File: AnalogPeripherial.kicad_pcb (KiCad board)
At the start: 2 copper layers, 48 parts, among them J1 USART, J2 SWD, J3 USB_B_Mini, SW3 SW_Nidec_CAS-120A1, U1 LD1117S33TR_SOT223, U2 STM32F373CCTx, U3 LM386, U4 112J-TDAR-R01, U5 TLV9061xDBV, Y1 Crystal

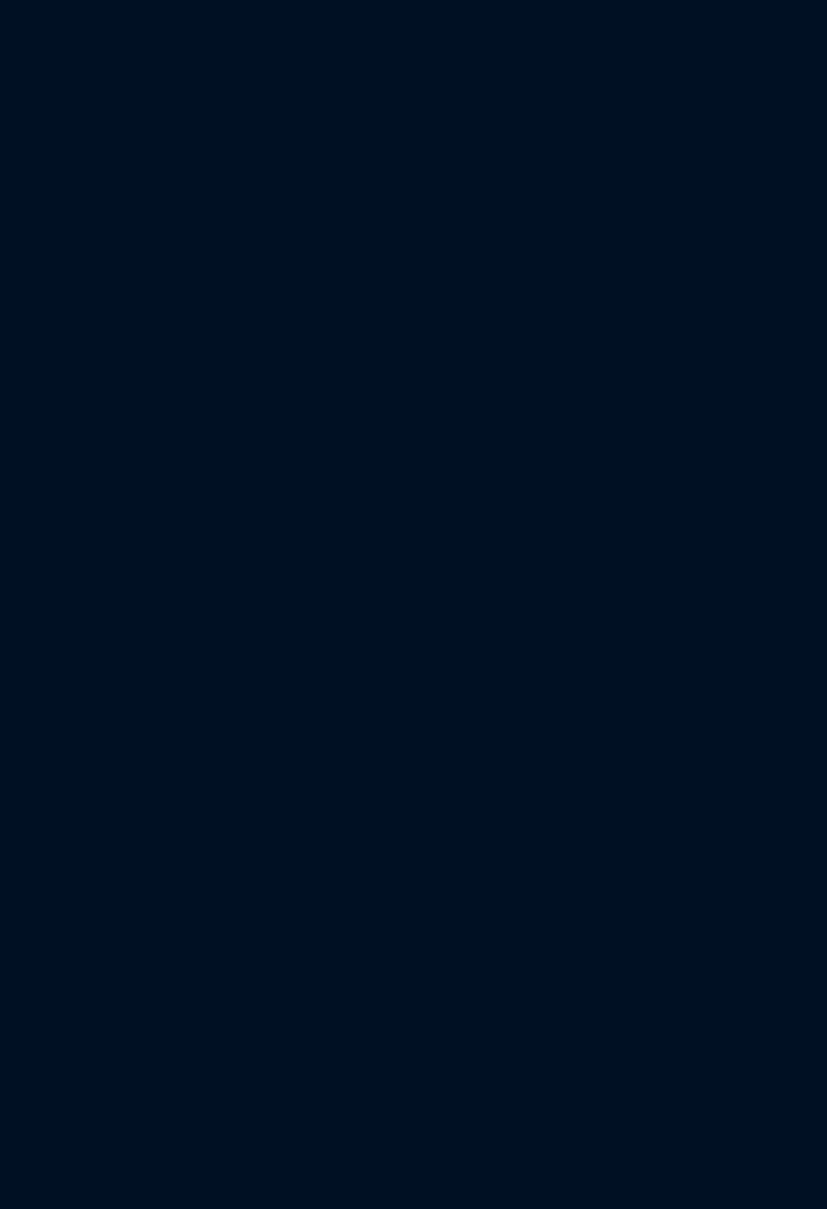
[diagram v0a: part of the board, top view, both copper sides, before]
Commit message: Add all footprint To do: 1. Add footprint and symbol to SD Card 2. Correct footprints and symobols 3. Finish the PCB design
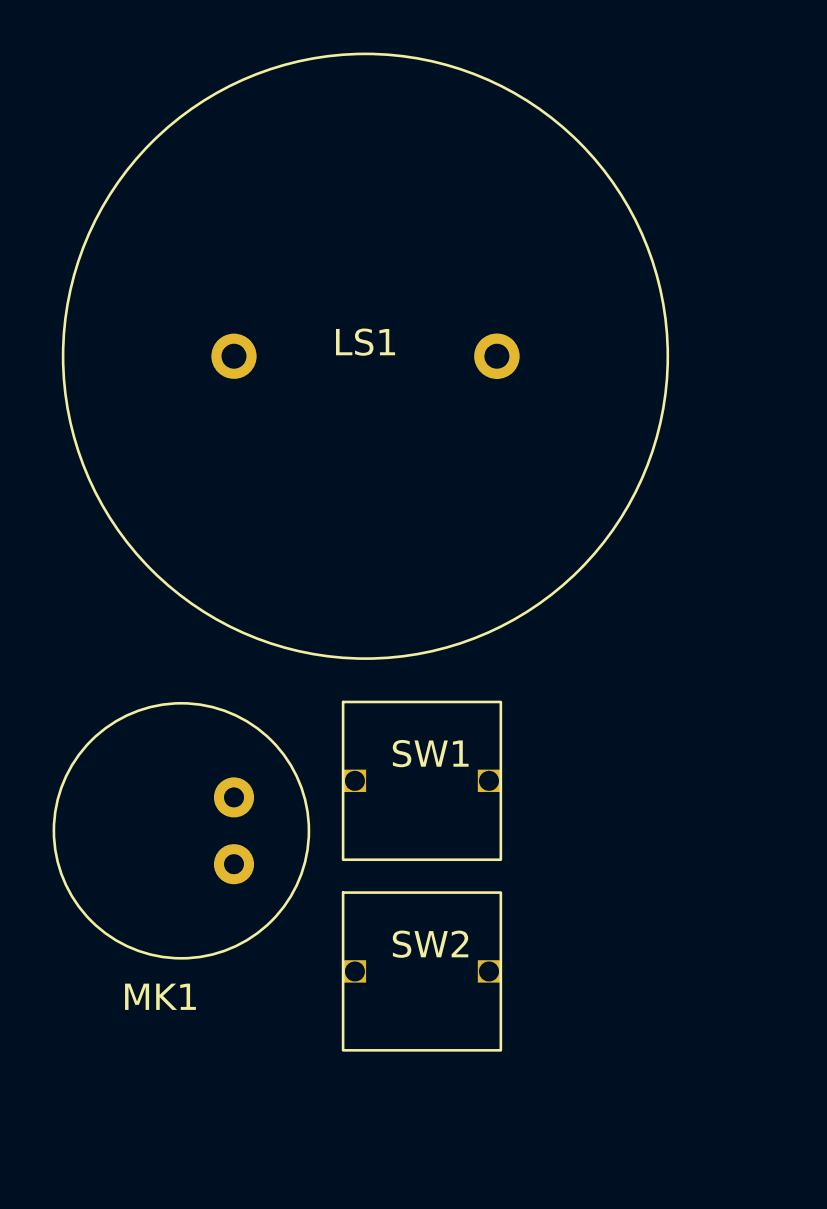
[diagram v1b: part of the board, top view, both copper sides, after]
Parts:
- added LS1: Speaker, my_custom_stuff:speaker, F.Cu at (61.5, 57.4)
- added MK1: Microphone, my_custom_stuff:microphone, F.Cu at (54.5, 75.4)
- added SW1: record, my_custom_stuff:button, F.Cu at (63.7, 73.5)
- added SW2: replay, my_custom_stuff:button, F.Cu at (63.7, 80.8)

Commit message: PCB progress
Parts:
- U4: value 112J-TDAR-R01 -> ~; footprint 112J_TDAR_R01:112J-TDAR-R01_ATT -> my_custom_stuff:microSD
- Y1: footprint Crystal:Crystal_HC18-U_Vertical -> Crystal:Crystal_HC49-4H_Vertical
- moved LS1 90.7 mm to (121.8, 125.2)
- moved SW1 90.0 mm to (148.4, 103.8)
- moved SW2 89.9 mm to (148.4, 111.0)
- moved MK1 78.4 mm to (132.8, 70.8), turned to -90 degrees
- moved J1 75.8 mm to (158.0, 100.1), turned to 180 degrees
- moved J2 72.6 mm to (157.8, 86.9), turned to 180 degrees
- moved SW3 72.0 mm to (157.8, 73.2)
- moved R1 68.8 mm to (157.1, 119.2), turned to 0 degrees
- moved U1 64.4 mm to (151.8, 127.4), turned to -90 degrees
- moved C9 62.0 mm to (153.1, 121.7), turned to 0 degrees
- moved D1 60.5 mm to (153.1, 119.2), turned to 180 degrees
- moved C3 56.9 mm to (150.5, 66.8)
- moved C4 53.2 mm to (148.3, 121.7), turned to 180 degrees
- moved C6 51.0 mm to (143.5, 66.6), turned to 180 degrees
- moved Y1 48.0 mm to (149.3, 70.8), turned to 180 degrees
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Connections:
- net USART_RX renamed USART1_RX
- net USART_TX renamed USART1_TX
- U2 pad 10: ADC1_IN1 -> unconnected-(U2-PA0-Pad10)
- U2 pad 11: unconnected-(U2-PA1-Pad11) -> ADC1_IN1
- U4 pad 1: SPI1_NSS -> unconnected-(U4-DAT2-Pad1)
- U4 pad 2: SPI1_MISO -> SPI1_NSS
- U4 pad 3: GND -> SPI1_MOSI
- U4 pad 6: unconnected-(U4-Pad6) -> GND
- U4 pad 7: SPI1_MOSI -> SPI1_MISO
- U4 pad 9: unconnected-(U4-Pad9) -> (no net)

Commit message: PCB design still in progress
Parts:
- added C23: 33p, Capacitor_SMD:C_0805_2012Metric_Pad1.18x1.45mm_HandSolder, F.Cu at (124.0, 70.0)
- added C24: 10u, Capacitor_SMD:C_0805_2012Metric_Pad1.18x1.45mm_HandSolder, F.Cu at (83.2, 110.0)
- C16: value 100p -> 100u
- C17: value 0.047u -> 0.05u
- C18: value 470u -> 250u
- C19: value 330n -> 68n
- C20: value 47u -> 40u
- C21: value 120p -> 995p
- C22: value 3.3u -> 150n
- R11: value 10k -> 100
- R6: value 5.9k -> 2.2k
- R7, R8: value 200k -> 100k
- R9: value 787 -> 78.7
- moved C18 42.5 mm to (91.0, 117.0)
- moved R5 41.1 mm to (96.5, 117.8)
- moved C16 41.1 mm to (95.5, 112.1)
- moved RV1 40.9 mm to (82.5, 113.0)
- moved C15 40.9 mm to (89.4, 108.5)
- moved U3 40.9 mm to (89.3, 112.6)
- moved C17 40.9 mm to (95.5, 114.6)
- moved LS1 33.0 mm to (89.5, 131.6)
- moved R1 30.3 mm to (143.5, 146.3), turned to -90 degrees
- moved C9 29.4 mm to (140.2, 148.1)
- moved D1 29.4 mm to (140.2, 145.6)
- moved U1 29.3 mm to (139.2, 153.8)
- moved C4 29.3 mm to (135.8, 148.1)
- moved SW1 27.5 mm to (172.4, 117.3), turned to 180 degrees
- moved R2 25.2 mm to (128.7, 148.6)
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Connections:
- net /NRST renamed Net-(U2-NRST)
- C22 pad 1: Net-(C21-Pad2) -> GND
- R11 pad 1: GND -> ADC1_IN1
- R11 pad 2: ADC1_IN1 -> Net-(C21-Pad2)
- RV1 pad 1: DAC1_OUT1 -> Net-(C24-Pad2)
- U2 pad 1: GND -> 3V3
- U2 pad 17: GND -> 3V3
- U2 pad 21: unconnected-(U2-PE8-Pad21) -> SPI1_NSS
- U2 pad 24: GND -> 3VA3
- U2 pad 38: SPI1_NSS -> unconnected-(U2-PA15-Pad38)
- U2 pad 48: GND -> 3V3
- U2 pad 9: GND -> 3VA3
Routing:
- net 3V3: track 0.00 -> 145.5 mm, vias 0 -> 5
- net USB+: track 0.00 -> 25.7 mm
- net USB-: track 0.00 -> 23.2 mm
- net BOOT0: track 0.00 -> 21.9 mm
- net SPI1_SCK: track 0.00 -> 21.1 mm, vias 0 -> 2
- net USART1_TX: track 0.00 -> 20.0 mm, vias 0 -> 1
- net DAC1_OUT1: track 0.00 -> 19.9 mm, vias 0 -> 2
- net SPI1_MOSI: track 0.00 -> 18.5 mm
- net USART1_RX: track 0.00 -> 18.1 mm, vias 0 -> 1
- net SPI1_NSS: track 0.00 -> 18.0 mm
- net SWDIO: track 0.00 -> 17.6 mm, vias 0 -> 1
- net VBUS: track 0.00 -> 17.5 mm
- net ADC1_IN1: track 0.00 -> 17.2 mm
- net HSE_IN: track 0.00 -> 17.2 mm
- net SPI1_MISO: track 0.00 -> 17.1 mm
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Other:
- board outline added: 52 x 73.6 mm
